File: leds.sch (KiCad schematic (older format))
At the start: 11 parts, among them IC2 IS31FL3199

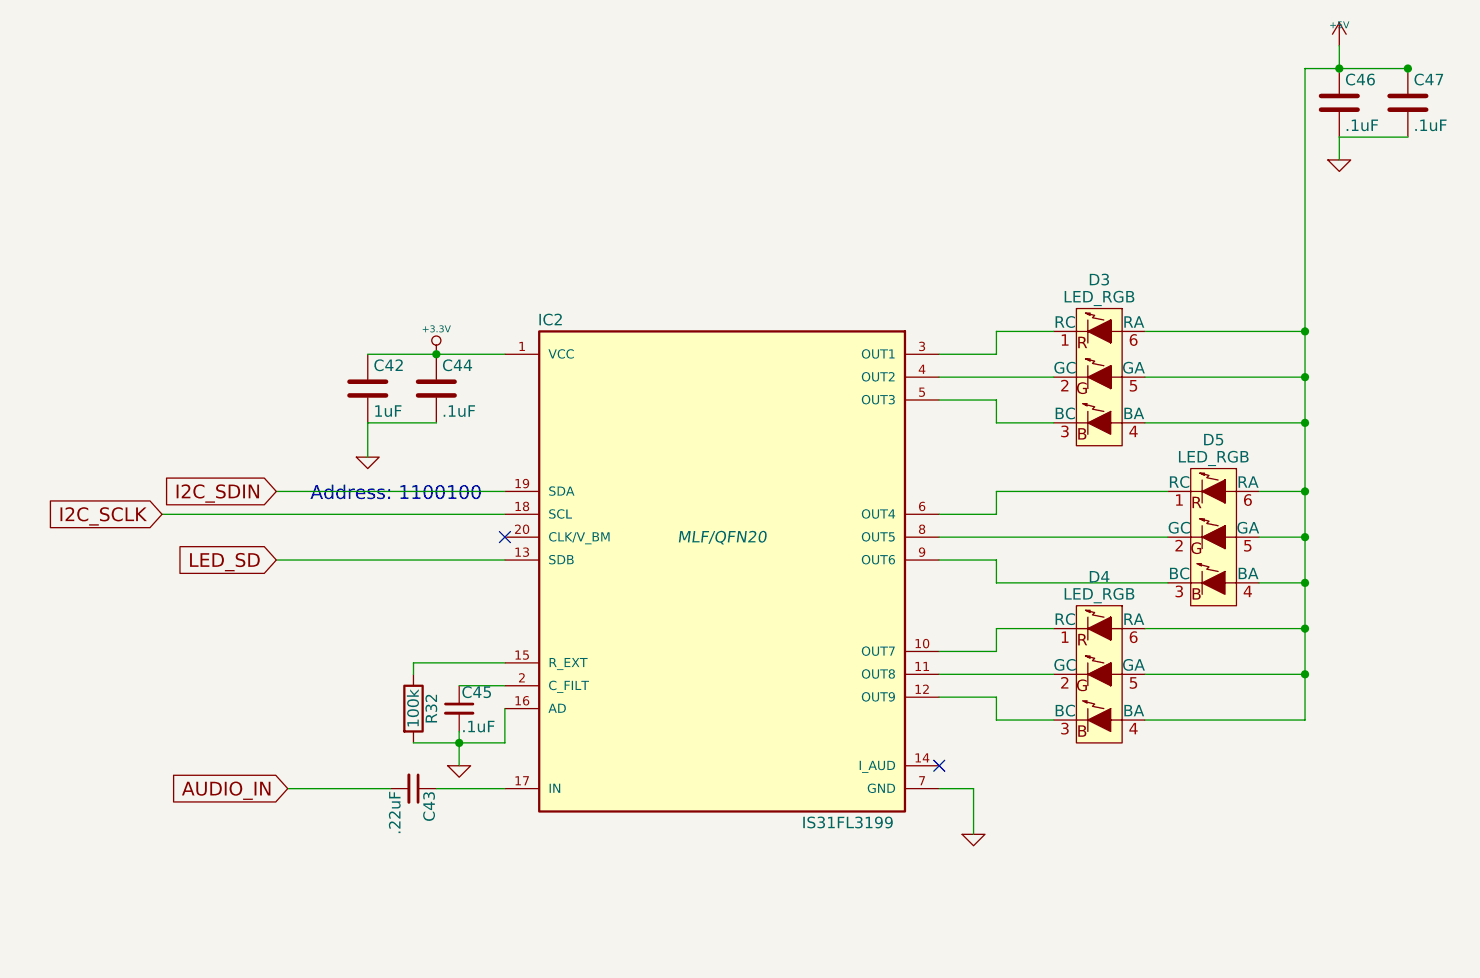
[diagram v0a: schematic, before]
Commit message: resolved ERC errors, and began assigning footprints
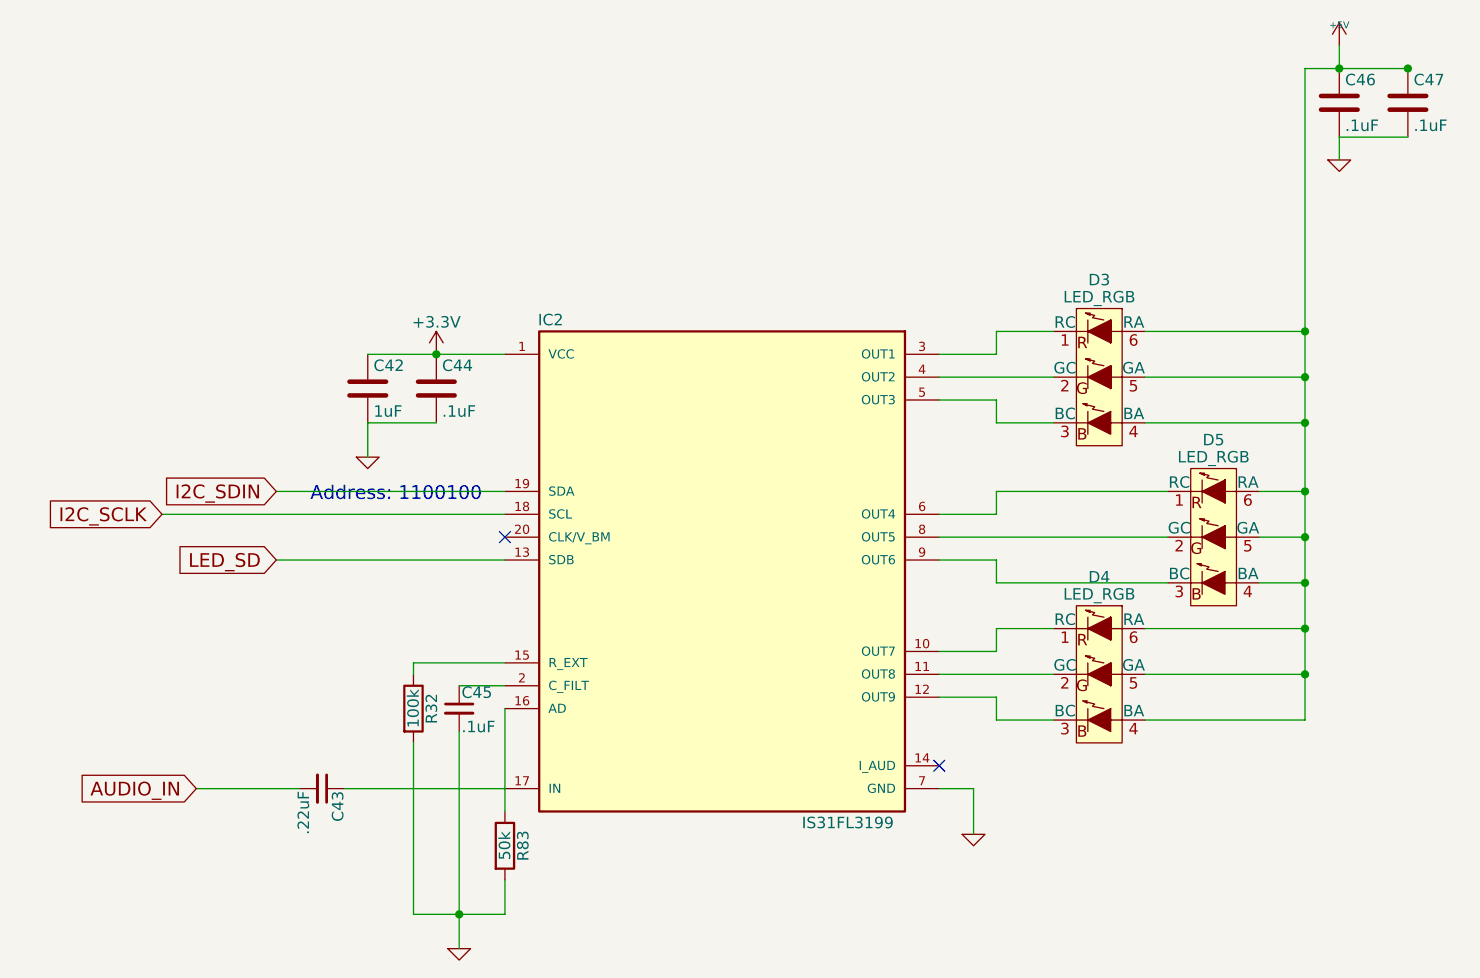
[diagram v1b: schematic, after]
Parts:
- added R83: 50k, symbol R
- C42, C44, C45, C46, C47: footprint (none) -> Capacitors_SMD:C_0603
- IC2: footprint MLF/QFN20 -> (none)
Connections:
- net GND: now also R83.2; no longer IC2.16 (AD)
- net +3.3V renamed +3V3
- new net: IC2.16 (AD), R83.1
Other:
- moved on the sheet: C43
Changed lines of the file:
@@
 LIBS:N25Q128A
 LIBS:sparkfun
+LIBS:GSB3211311WEU
+LIBS:48258-0001
+LIBS:ArduinoSpecAn-cache
+LIBS:passiveelectret
+LIBS:passiveind
+LIBS:passiveinductor
+LIBS:fb_powerout
+LIBS:ferrite
+LIBS:df_device
 EELAYER 25 0
 EELAYER END
@@
 F 0 "IC2" H 3300 5350 50  0000 C CNN
 F 1 "IS31FL3199" H 4600 3150 50  0000 C CNN
-F 2 "MLF/QFN20" H 4050 4400 50  0000 C CIN
+F 2 "" H 4050 4400 50  0001 C CIN
 F 3 "" H 4050 4600 50  0000 C CNN
 	1    4050 4150
@@
 F 0 "C44" H 2825 3350 50  0000 L CNN
 F 1 ".1uF" H 2825 3150 50  0000 L CNN
-F 2 "" H 2838 3100 50  0000 C CNN
+F 2 "Capacitors_SMD:C_0603" H 2838 3100 50  0001 C CNN
 F 3 "" H 2800 3250 50  0000 C CNN
 	1    2800 3250
@@
 F 0 "C42" H 2525 3350 50  0000 L CNN
 F 1 "1uF" H 2525 3150 50  0000 L CNN
-F 2 "" H 2538 3100 50  0000 C CNN
+F 2 "Capacitors_SMD:C_0603" H 2538 3100 50  0001 C CNN
 F 3 "" H 2500 3250 50  0000 C CNN
 	1    2500 3250
@@
 $EndComp
 $Comp
-L GND-RESCUE-DFTBoard #PWR034
+L GND-RESCUE-DFTBoard #PWR038
 U 1 1 585893DE
 P 2500 3550
-F 0 "#PWR034" H 2500 3550 30  0001 C CNN
+F 0 "#PWR038" H 2500 3550 30  0001 C CNN
 F 1 "GND" H 2500 3480 30  0001 C CNN
 F 2 "" H 2500 3550 60  0001 C CNN
@@
 F 0 "D3" H 5700 3625 50  0000 C CNN
 F 1 "LED_RGB" H 5700 3550 50  0000 C CNN
-F 2 "" H 5700 3150 50  0000 C CNN
+F 2 "" H 5700 3150 50  0001 C CNN
 F 3 "" H 5700 3150 50  0000 C CNN
 	1    5700 3200
@@
 F 0 "D5" H 6200 4325 50  0000 C CNN
 F 1 "LED_RGB" H 6200 4250 50  0000 C CNN
-F 2 "" H 6200 3850 50  0000 C CNN
+F 2 "" H 6200 3850 50  0001 C CNN
 F 3 "" H 6200 3850 50  0000 C CNN
 	1    6200 3900
@@
 F 0 "D4" H 5700 4925 50  0000 C CNN
 F 1 "LED_RGB" H 5700 4850 50  0000 C CNN
-F 2 "" H 5700 4450 50  0000 C CNN
+F 2 "" H 5700 4450 50  0001 C CNN
 F 3 "" H 5700 4450 50  0000 C CNN
 	1    5700 4500
@@
 Wire Wire Line
 	5250 4700 5500 4700
-$Comp
-L +3.3V-RESCUE-DFTBoard #PWR035
-U 1 1 5858AA08
-P 2800 3100
-F 0 "#PWR035" H 2800 3060 30  0001 C CNN
-F 1 "+3.3V" H 2800 3210 30  0000 C CNN
-F 2 "" H 2800 3100 60  0001 C CNN
-F 3 "" H 2800 3100 60  0001 C CNN
-	1    2800 3100
-	1    0    0    -1
-$EndComp
 Wire Wire Line
 	5250 3000 5500 3000
 $Comp
-L GND-RESCUE-DFTBoard #PWR036
+L GND-RESCUE-DFTBoard #PWR039
 U 1 1 5858ACBB
 P 5150 5200
-F 0 "#PWR036" H 5150 5200 30  0001 C CNN
+F 0 "#PWR039" H 5150 5200 30  0001 C CNN
 F 1 "GND" H 5150 5130 30  0001 C CNN
 F 2 "" H 5150 5200 60  0001 C CNN
@@
 	5150 5000 5150 5200
 $Comp
-L GND-RESCUE-DFTBoard #PWR037
+L GND-RESCUE-DFTBoard #PWR040
 U 1 1 5858AD21
-P 2900 4900
-F 0 "#PWR037" H 2900 4900 30  0001 C CNN
-F 1 "GND" H 2900 4830 30  0001 C CNN
-F 2 "" H 2900 4900 60  0001 C CNN
-F 3 "" H 2900 4900 60  0001 C CNN
-	1    2900 4900
+P 2900 5700
+F 0 "#PWR040" H 2900 5700 30  0001 C CNN
+F 1 "GND" H 2900 5630 30  0001 C CNN
+F 2 "" H 2900 5700 60  0001 C CNN
+F 3 "" H 2900 5700 60  0001 C CNN
+	1    2900 5700
 	1    0    0    -1
 $EndComp
@@
 F 0 "C45" H 2910 4720 50  0000 L CNN
 F 1 ".1uF" H 2910 4570 50  0000 L CNN
-F 2 "" H 2900 4650 50  0000 C CNN
+F 2 "Capacitors_SMD:C_0603" H 2900 4650 50  0001 C CNN
 F 3 "" H 2900 4650 50  0000 C CNN
 	1    2900 4650
@@
 Wire Wire Line
 	3100 4550 2900 4550
-Wire Wire Line
-	3100 4800 3100 4650
-Wire Wire Line
-	2700 4800 3100 4800
-Connection ~ 2900 4800
 $Comp
 L R R32
@@
 F 0 "R32" V 2780 4650 50  0000 C CNN
 F 1 "100k" V 2700 4650 50  0000 C CNN
-F 2 "" V 2630 4650 50  0000 C CNN
+F 2 "" V 2630 4650 50  0001 C CNN
 F 3 "" H 2700 4650 50  0000 C CNN
 	1    2700 4650
@@
 	2700 4450 2700 4500
 Wire Wire Line
-	2900 4750 2900 4900
-Text GLabel 2150 5000 0    60   Input ~ 0
+	2900 4750 2900 5700
+Text GLabel 1750 5000 0    60   Input ~ 0
 AUDIO_IN
 $Comp
 L C_Small C43
 U 1 1 5858C490
-P 2700 5000
-F 0 "C43" H 2710 5070 50  0000 L CNN
-F 1 ".22uF" H 2710 4920 50  0000 L CNN
-F 2 "" H 2700 5000 50  0000 C CNN
-F 3 "" H 2700 5000 50  0000 C CNN
-	1    2700 5000
+P 2300 5000
+F 0 "C43" H 2310 5070 50  0000 L CNN
+F 1 ".22uF" H 2310 4920 50  0000 L CNN
+F 2 "" H 2300 5000 50  0001 C CNN
+F 3 "" H 2300 5000 50  0000 C CNN
+	1    2300 5000
 	0    1    1    0
 $EndComp
 Wire Wire Line
-	3100 5000 2800 5000
-Wire Wire Line
-	2600 5000 2150 5000
+	2400 5000 3100 5000
+Wire Wire Line
+	2200 5000 1750 5000
 $Comp
 L C C46
@@
 F 0 "C46" H 6775 2100 50  0000 L CNN
 F 1 ".1uF" H 6775 1900 50  0000 L CNN
-F 2 "" H 6788 1850 50  0000 C CNN
+F 2 "Capacitors_SMD:C_0603" H 6788 1850 50  0001 C CNN
 F 3 "" H 6750 2000 50  0000 C CNN
 	1    6750 2000
@@
 F 0 "C47" H 7075 2100 50  0000 L CNN
 F 1 ".1uF" H 7075 1900 50  0000 L CNN
-F 2 "" H 7088 1850 50  0000 C CNN
+F 2 "Capacitors_SMD:C_0603" H 7088 1850 50  0001 C CNN
 F 3 "" H 7050 2000 50  0000 C CNN
 	1    7050 2000
@@
 $EndComp
 $Comp
-L +5V #PWR038
+L +5V #PWR041
 U 1 1 5858D0D0
 P 6750 1750
-F 0 "#PWR038" H 6750 1840 20  0001 C CNN
+F 0 "#PWR041" H 6750 1840 20  0001 C CNN
 F 1 "+5V" H 6750 1840 30  0000 C CNN
 F 2 "" H 6750 1750 60  0001 C CNN
@@
 Connection ~ 6750 1850
 $Comp
-L GND-RESCUE-DFTBoard #PWR039
+L GND-RESCUE-DFTBoard #PWR042
 U 1 1 5858E9FF
 P 6750 2250
-F 0 "#PWR039" H 6750 2250 30  0001 C CNN
+F 0 "#PWR042" H 6750 2250 30  0001 C CNN
 F 1 "GND" H 6750 2180 30  0001 C CNN
 F 2 "" H 6750 2250 60  0001 C CNN
@@
 NoConn ~ 5000 4900
 NoConn ~ 3100 3900
+$Comp
+L R R83
+U 1 1 5870DDC1
+P 3100 5250
+F 0 "R83" V 3180 5250 50  0000 C CNN
+F 1 "50k" V 3100 5250 50  0000 C CNN
+F 2 "" V 3030 5250 50  0001 C CNN
+F 3 "" H 3100 5250 50  0000 C CNN
+	1    3100 5250
+	1    0    0    -1
+$EndComp
+Wire Wire Line
+	3100 5550 3100 5400
+Wire Wire Line
+	2700 5550 3100 5550
+Wire Wire Line
+	2700 4800 2700 5550
+Connection ~ 2900 5550
+Wire Wire Line
+	3100 4650 3100 5100
+$Comp
+L +3.3V #PWR043
+U 1 1 58742E81
+P 2800 3100
+F 0 "#PWR043" H 2800 2950 50  0001 C CNN
+F 1 "+3.3V" H 2800 3240 50  0000 C CNN
+F 2 "" H 2800 3100 50  0000 C CNN
+F 3 "" H 2800 3100 50  0000 C CNN
+	1    2800 3100
+	1    0    0    -1
+$EndComp
 $EndSCHEMATC

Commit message: a few more footprints
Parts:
- C43: footprint (none) -> Capacitors_SMD:C_0402
- D3, D4, D5: footprint (none) -> led:PLCC6-SM-RGB-LED
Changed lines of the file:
@@
 $EndComp
 $Comp
-L GND-RESCUE-DFTBoard #PWR37
+L GND-RESCUE-DFTBoard #PWR038
 U 1 1 585893DE
 P 2500 3550
-F 0 "#PWR37" H 2500 3550 30  0001 C CNN
+F 0 "#PWR038" H 2500 3550 30  0001 C CNN
 F 1 "GND" H 2500 3480 30  0001 C CNN
 F 2 "" H 2500 3550 60  0001 C CNN
@@
 F 0 "D3" H 5700 3625 50  0000 C CNN
 F 1 "LED_RGB" H 5700 3550 50  0000 C CNN
-F 2 "" H 5700 3150 50  0001 C CNN
+F 2 "led:PLCC6-SM-RGB-LED" H 5700 3150 50  0001 C CNN
 F 3 "" H 5700 3150 50  0000 C CNN
 	1    5700 3200
@@
 F 0 "D5" H 6200 4325 50  0000 C CNN
 F 1 "LED_RGB" H 6200 4250 50  0000 C CNN
-F 2 "" H 6200 3850 50  0001 C CNN
+F 2 "led:PLCC6-SM-RGB-LED" H 6200 3850 50  0001 C CNN
 F 3 "" H 6200 3850 50  0000 C CNN
 	1    6200 3900
@@
 F 0 "D4" H 5700 4925 50  0000 C CNN
 F 1 "LED_RGB" H 5700 4850 50  0000 C CNN
-F 2 "" H 5700 4450 50  0001 C CNN
+F 2 "led:PLCC6-SM-RGB-LED" H 5700 4450 50  0001 C CNN
 F 3 "" H 5700 4450 50  0000 C CNN
 	1    5700 4500
@@
 	5250 3000 5500 3000
 $Comp
-L GND-RESCUE-DFTBoard #PWR40
+L GND-RESCUE-DFTBoard #PWR039
 U 1 1 5858ACBB
 P 5150 5200
-F 0 "#PWR40" H 5150 5200 30  0001 C CNN
+F 0 "#PWR039" H 5150 5200 30  0001 C CNN
 F 1 "GND" H 5150 5130 30  0001 C CNN
 F 2 "" H 5150 5200 60  0001 C CNN
@@
 	5150 5000 5150 5200
 $Comp
-L GND-RESCUE-DFTBoard #PWR39
+L GND-RESCUE-DFTBoard #PWR040
 U 1 1 5858AD21
 P 2900 5700
-F 0 "#PWR39" H 2900 5700 30  0001 C CNN
+F 0 "#PWR040" H 2900 5700 30  0001 C CNN
 F 1 "GND" H 2900 5630 30  0001 C CNN
 F 2 "" H 2900 5700 60  0001 C CNN
@@
 F 0 "C43" H 2310 5070 50  0000 L CNN
 F 1 ".22uF" H 2310 4920 50  0000 L CNN
-F 2 "" H 2300 5000 50  0001 C CNN
+F 2 "Capacitors_SMD:C_0402" H 2300 5000 50  0001 C CNN
 F 3 "" H 2300 5000 50  0000 C CNN
 	1    2300 5000
@@
 $EndComp
 $Comp
-L +5V #PWR41
+L +5V #PWR041
 U 1 1 5858D0D0
 P 6750 1750
-F 0 "#PWR41" H 6750 1840 20  0001 C CNN
+F 0 "#PWR041" H 6750 1840 20  0001 C CNN
 F 1 "+5V" H 6750 1840 30  0000 C CNN
 F 2 "" H 6750 1750 60  0001 C CNN
@@
 Connection ~ 6750 1850
 $Comp
-L GND-RESCUE-DFTBoard #PWR42
+L GND-RESCUE-DFTBoard #PWR042
 U 1 1 5858E9FF
 P 6750 2250
-F 0 "#PWR42" H 6750 2250 30  0001 C CNN
+F 0 "#PWR042" H 6750 2250 30  0001 C CNN
 F 1 "GND" H 6750 2180 30  0001 C CNN
 F 2 "" H 6750 2250 60  0001 C CNN
@@
 	3100 4650 3100 5100
 $Comp
-L +3.3V #PWR38
+L +3.3V #PWR043
 U 1 1 58742E81
 P 2800 3100
-F 0 "#PWR38" H 2800 2950 50  0001 C CNN
+F 0 "#PWR043" H 2800 2950 50  0001 C CNN
 F 1 "+3.3V" H 2800 3240 50  0000 C CNN
 F 2 "" H 2800 3100 50  0000 C CNN

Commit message: A few more footprints
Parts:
- IC2: footprint (none) -> QFN-20-4MM:QFN-20-4MM
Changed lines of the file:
@@
 F 0 "IC2" H 3300 5350 50  0000 C CNN
 F 1 "IS31FL3199" H 4600 3150 50  0000 C CNN
-F 2 "" H 4050 4400 50  0001 C CIN
+F 2 "QFN-20-4MM:QFN-20-4MM" H 4050 4400 50  0001 C CIN
 F 3 "" H 4050 4600 50  0000 C CNN
 	1    4050 4150

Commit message: added resistor footprints (1206)
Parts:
- R32, R83: footprint (none) -> Resistors_SMD:R_1206
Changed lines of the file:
@@
 F 0 "R32" V 2780 4650 50  0000 C CNN
 F 1 "100k" V 2700 4650 50  0000 C CNN
-F 2 "" V 2630 4650 50  0001 C CNN
+F 2 "Resistors_SMD:R_1206" V 2630 4650 50  0001 C CNN
 F 3 "" H 2700 4650 50  0000 C CNN
 	1    2700 4650
@@
 F 0 "R83" V 3180 5250 50  0000 C CNN
 F 1 "50k" V 3100 5250 50  0000 C CNN
-F 2 "" V 3030 5250 50  0001 C CNN
+F 2 "Resistors_SMD:R_1206" V 3030 5250 50  0001 C CNN
 F 3 "" H 3100 5250 50  0000 C CNN
 	1    3100 5250

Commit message: fixed a few diagram/footprint pin mismatches, getting ready to pull gene's microhdmi footprint
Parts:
- D3, D4, D5: footprint led:PLCC6-SM-RGB-LED -> DFTcustom:PLCC6-SM-RGB-LED
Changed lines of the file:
@@
 LIBS:ferrite
 LIBS:df_device
+LIBS:JACK_TRS_5PINS
 EELAYER 25 0
 EELAYER END
@@
 F 0 "D3" H 5700 3625 50  0000 C CNN
 F 1 "LED_RGB" H 5700 3550 50  0000 C CNN
-F 2 "led:PLCC6-SM-RGB-LED" H 5700 3150 50  0001 C CNN
+F 2 "DFTcustom:PLCC6-SM-RGB-LED" H 5700 3150 50  0001 C CNN
 F 3 "" H 5700 3150 50  0000 C CNN
 	1    5700 3200
@@
 F 0 "D5" H 6200 4325 50  0000 C CNN
 F 1 "LED_RGB" H 6200 4250 50  0000 C CNN
-F 2 "led:PLCC6-SM-RGB-LED" H 6200 3850 50  0001 C CNN
+F 2 "DFTcustom:PLCC6-SM-RGB-LED" H 6200 3850 50  0001 C CNN
 F 3 "" H 6200 3850 50  0000 C CNN
 	1    6200 3900
@@
 F 0 "D4" H 5700 4925 50  0000 C CNN
 F 1 "LED_RGB" H 5700 4850 50  0000 C CNN
-F 2 "led:PLCC6-SM-RGB-LED" H 5700 4450 50  0001 C CNN
+F 2 "DFTcustom:PLCC6-SM-RGB-LED" H 5700 4450 50  0001 C CNN
 F 3 "" H 5700 4450 50  0000 C CNN
 	1    5700 4500
